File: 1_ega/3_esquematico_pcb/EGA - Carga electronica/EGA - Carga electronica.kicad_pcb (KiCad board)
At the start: 2 copper layers, 100 x 100 mm, 55 parts, among them J1 LCD20x4, J2 DS3231, J3 ENCODER, J4 I2C1_Reservado, J5 UART0_Reservado, J6 Conn_01x03, J7 Ventrada, Q1 IRLZ44N, SW1 SW_Push, SW2 SW_Push, U1 Pico, U2 LM7805_TO220, U3 TL082, U4 TL082

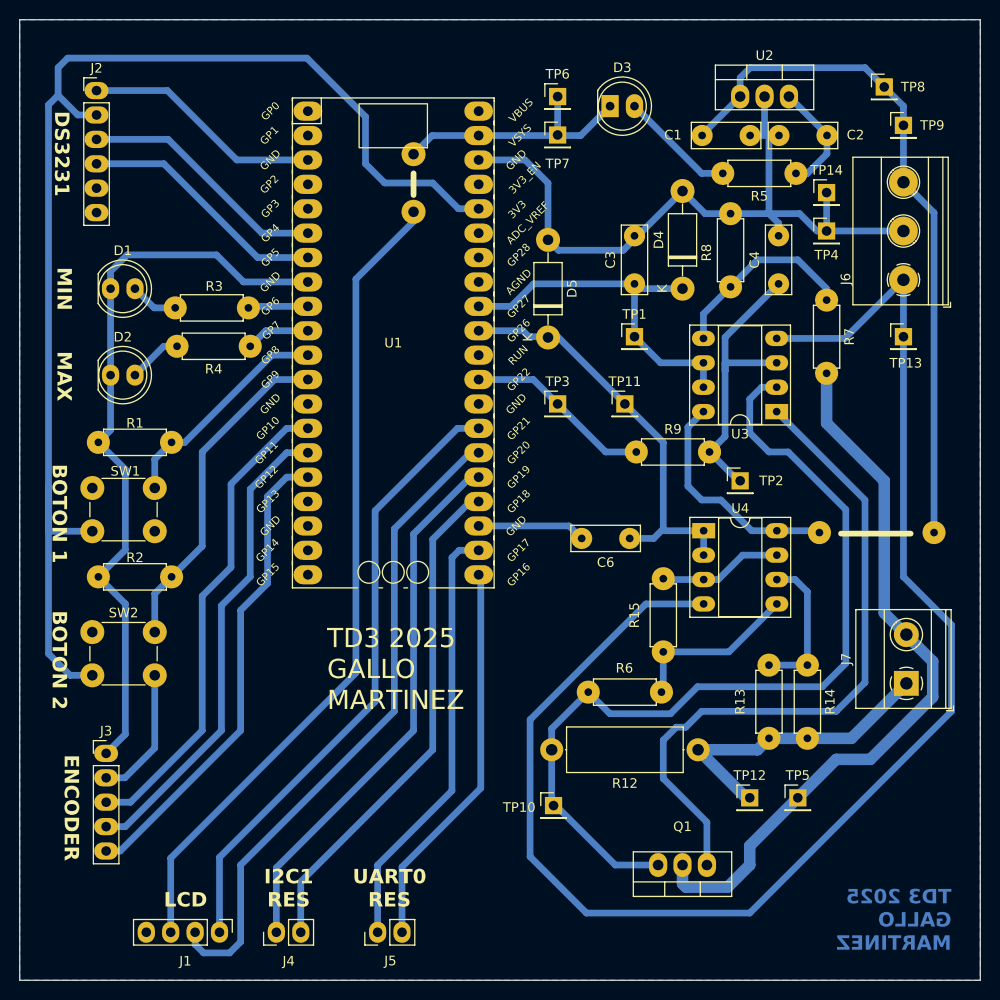
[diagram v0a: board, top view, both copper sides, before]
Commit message: Se agrega task_Sensado
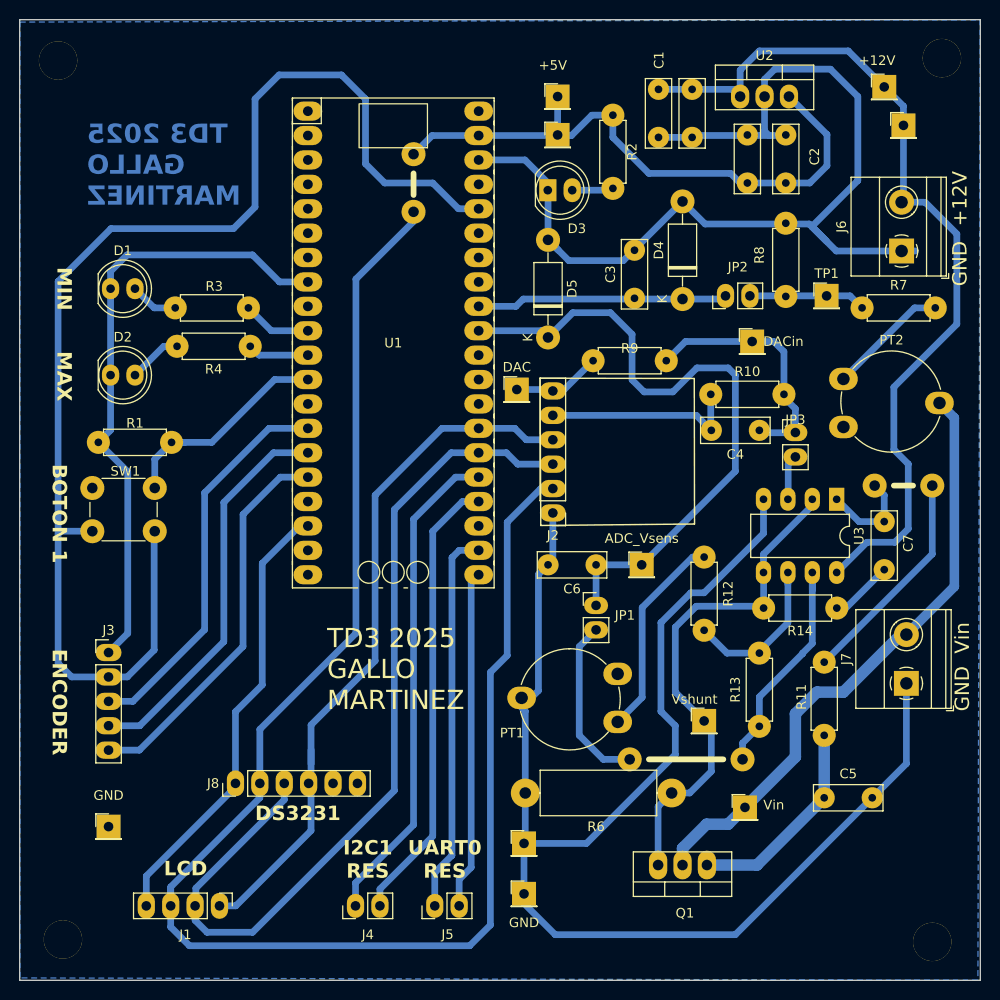
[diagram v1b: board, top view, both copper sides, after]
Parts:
- removed the ? at (125.2, 95.4)
- removed the ? at (113.3, 95.4)
- removed R15: 10K, Resistor_THT:R_Axial_DIN0207_L6.3mm_D2.5mm_P7.62mm_Horizontal
- removed R5: 1K, Resistor_THT:R_Axial_DIN0207_L6.3mm_D2.5mm_P7.62mm_Horizontal
- removed SW2: SW_Push, Button_Switch_THT:SW_PUSH_6mm_H5mm
- removed TP13: -12V, Connector_PinHeader_2.54mm:PinHeader_1x01_P2.54mm_Vertical
- removed U4: TL082, Package_DIP:DIP-8_W7.62mm_Socket_LongPads
- added ?: , , F.Cu at (105.2, 119.0)
- added ?: , , F.Cu at (125.0, 138.0)
- added ?: , , F.Cu at (34.0, 46.2)
- added ?: , , F.Cu at (119.0, 90.5)
- added ?: , , F.Cu at (34.5, 137.8)
- added ?: , , F.Cu at (127.0, 47.0)
- added ?: , , F.Cu at (125.0, 90.5)
- added ?: , , F.Cu at (93.5, 119.0)
- added C1: 0,33uF, Capacitor_THT:C_Disc_D7.0mm_W2.5mm_P5.00mm, F.Cu at (96.5, 49.2)
- added C2: 0,33uF, Capacitor_THT:C_Disc_D7.0mm_W2.5mm_P5.00mm, F.Cu at (105.8, 59.0)
- added C5: 10nF, Capacitor_THT:C_Disc_D7.0mm_W2.5mm_P5.00mm, F.Cu at (113.8, 123.0)
- added C7: 1nF, Capacitor_THT:C_Disc_D7.0mm_W2.5mm_P5.00mm, F.Cu at (120.0, 99.2)
- added J8: DS3231, Connector_PinHeader_2.54mm:PinHeader_1x06_P2.54mm_Vertical, F.Cu at (52.5, 121.5)
- added JP1: Jumper, Connector_PinHeader_2.54mm:PinHeader_1x02_P2.54mm_Vertical, F.Cu at (90.0, 103.0)
- added JP2: Jumper, Connector_PinHeader_2.54mm:PinHeader_1x02_P2.54mm_Vertical, F.Cu at (103.5, 70.8)
- added JP3: Jumper, Connector_PinHeader_2.54mm:PinHeader_1x02_P2.54mm_Vertical, F.Cu at (110.8, 85.0)
- added PT1: PRESET 1K, Potentiometer_THT:Potentiometer_Piher_PT-10-V10_Vertical, F.Cu at (92.2, 110.1)
- added PT2: PRESET 1K, Potentiometer_THT:Potentiometer_Piher_PT-10-V10_Vertical, F.Cu at (115.8, 84.4)
- added R10: 10K, Resistor_THT:R_Axial_DIN0207_L6.3mm_D2.5mm_P7.62mm_Horizontal, F.Cu at (101.9, 81.0)
- added R11: 100, Resistor_THT:R_Axial_DIN0207_L6.3mm_D2.5mm_P7.62mm_Horizontal, F.Cu at (113.8, 116.5)
- C4: value 33nF -> 100nF
- DAC: renamed from TP3; value PWM -> VDAC
- J2: value DS3231 -> MCP4725
- J6: value Conn_01x03 -> V+; footprint TerminalBlock_Phoenix:TerminalBlock_Phoenix_MKDS-1,5-3-5.08_1x03_P5.08mm_Horizontal -> TerminalBlock_Phoenix:TerminalBlock_Phoenix_MKDS-1,5-2-5.08_1x02_P5.08mm_Horizontal
- Q1: value IRLZ44N -> IRFZ44
- R12: value 27K -> 10K
- R13: value 27K -> 3,3K
- R2: value 10K -> 1K
- R7: value 27K -> 12K
- R8: value 10K -> 4,7K
- U3: value TL082 -> LM358; footprint Package_DIP:DIP-8_W7.62mm_Socket_LongPads -> Package_DIP:DIP-8_W7.62mm_LongPads
- moved TP14 79.5 mm to (82.5, 133.0)
- moved GND 71.1 mm to (82.5, 127.8)
- moved GND 66.8 mm to (39.2, 126.0)
- moved J2 64.7 mm to (85.5, 93.3), turned to 180 degrees
- moved R2 61.2 mm to (91.8, 59.6), turned to 90 degrees
- moved TP1 20.4 mm to (114.0, 70.8)
- moved Vshunt 18.0 mm to (101.2, 115.0)
- moved ADC_Vsens 16.8 mm to (94.8, 98.8)
- moved C4 15.4 mm to (107.0, 84.8), turned to 180 degrees
- moved R12 14.7 mm to (101.2, 97.9), turned to -90 degrees
- moved DACin 14.6 mm to (106.2, 75.5)
- moved R6 13.3 mm to (97.9, 122.5), turned to 180 degrees
- moved U3 11.1 mm to (115.0, 91.9), turned to -90 degrees
- moved D3 10.9 mm to (85.0, 59.8)
- moved R9 10.5 mm to (89.7, 77.5)
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- renumbered TP8 to +12V, TP6 to +5V, TP11 to ADC_Vsens, TP2 to DACin, TP4 to GND, TP12 to GND, TP5 to Vin, TP10 to Vshunt
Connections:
- C2 pad 1: Net-(U2-VO) -> +5V
- C4 pad 1: Net-(U3A-+) -> Net-(JP3-A)
- C4 pad 2: GND -> GND2
- D3 pad 1: +5V -> GND
- DAC pad 1: PWM_VSET -> DAC
- DACin pad 1: Net-(U3A-+) -> Net-(JP3-A)
- GND pad 1: GND2 -> GND
- J1 pad 1: SCL_LCD -> SCL_I2C0
- J1 pad 2: SDA_LCD -> SDA_I2C0
- J2 pad 2: +3.3V -> +5V
- J2 pad 3: SDA_DS3231 -> SDA_I2C0
- J2 pad 4: SCL_DS3231 -> SCL_I2C0
- J2 pad 5: unconnected-(J2-Pin_5-Pad5) -> GND2
- J2 pad 6: unconnected-(J2-Pin_6-Pad6) -> DAC
- J6 pad 1: -12V -> GND
- J6 pad 2: GND -> +12V
- J7 pad 1: GND2 -> GND
- R1 pad 1: SW_1 -> SW_CONFIG
- R12 pad 2: Net-(Q1-S) -> Net-(U3B--)
- R13 pad 1: Net-(U4B--) -> Net-(U3B--)
- R13 pad 2: GND2 -> Net-(JP1-B)
- R14 pad 1: Net-(U4B--) -> Net-(C7-Pad1)
- R14 pad 2: GND2 -> Net-(Q1-S)
- R2 pad 1: SW_2 -> Net-(D3-A)
- R2 pad 2: GND -> +5V
- R6 pad 2: GND2 -> GND
- R7 pad 1: Net-(U3B-+) -> Net-(JP2-B)
- R7 pad 2: /Vin -> Net-(PT2-Pad1)
- R8 pad 2: Net-(U3B-+) -> Net-(JP2-B)
- R9 pad 1: PWM_VSET -> DAC
- R9 pad 2: Net-(U3A-+) -> Net-(JP3-A)
- SW1 pad 1: SW_1 -> SW_CONFIG
- TP1 pad 1: ADC_VIN -> Net-(JP2-B)
- U1 pad 10: LED_MAX -> LED_MIN
- U1 pad 11: SW_1 -> LED_MAX
- U1 pad 12: SW_2 -> SW_CONFIG
- U1 pad 26: SDA_LCD -> SDA_I2C0
- U1 pad 27: SCL_LCD -> SCL_I2C0
- U1 pad 29: PWM_VSET -> unconnected-(U1-GPIO22-Pad29)
- U1 pad 6: SDA_DS3231 -> unconnected-(U1-GPIO4-Pad6)
- U1 pad 7: SCL_DS3231 -> unconnected-(U1-GPIO5-Pad7)
- U1 pad 9: LED_MIN -> unconnected-(U1-GPIO6-Pad9)
- U2 pad 3: Net-(U2-VO) -> +5V
- U3 pad 1: Net-(Q1-G) -> Net-(C7-Pad2)
- U3 pad 3: Net-(U3A-+) -> Net-(JP3-B)
- U3 pad 4: -12V -> GND
- U3 pad 5: Net-(U3B-+) -> Net-(Q1-S)
- U3 pad 6: ADC_VIN -> Net-(U3B--)
- U3 pad 7: ADC_VIN -> Net-(JP1-B)
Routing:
- net GND: track 191.7 -> 370.1 mm
- net -12V: track 155.0 -> 0.00 mm
- net +5V: track 112.0 -> 233.1 mm
- net SDA_I2C0: track 0.00 -> 94.9 mm
- net SCL_I2C0: track 0.00 -> 73.8 mm
- net SDA_LCD: track 68.5 -> 0.00 mm
- net SCL_LCD: track 64.9 -> 0.00 mm
- net Net-(Q1-G): track 70.4 -> 21.6 mm
- net Net-(JP1-B): track 0.00 -> 41.9 mm
- net Net-(Q1-S): track 92.8 -> 54.0 mm
- net SW_2: track 34.9 -> 0.00 mm
- net Net-(C7-Pad2): track 0.00 -> 33.1 mm
- net Net-(U3A-+): track 31.1 -> 0.00 mm
- net SCL_DS3231: track 26.0 -> 0.00 mm
- net SDA_DS3231: track 26.0 -> 0.00 mm
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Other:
- board text added: "+12V"
- board text added: "GND"
- board text added: "Vin"
- board text removed: "BOTON 2"
